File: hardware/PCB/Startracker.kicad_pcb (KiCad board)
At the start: 4 copper layers, 112 parts, among them IC1 IIS2MDCTR, IC2 BNO085, J1 GPS, J2 LoRa_prog, J3 Motor1, J4 Motor2, J5 Motor3, J6 6V, J7 SJ-3523-SMT-TR, J8 USB_C_Receptacle_USB2.0_16P, Q1 2N3904, Q2 2N3904, SW1 RST, SW2 BOOT, SW3 PWR, U1 ESP32-S3-WROOM-1, U10 TPS2121RUXR, U11 INA219BxDCN, U2 TMC2209-LA, U3 TB6612FNG, U4 TB6612FNG, U6 INA219BxDCN, U7 WLR089U0-I_RM, U8 SRV05-4, U9 TPS54308, Y1 Crystal

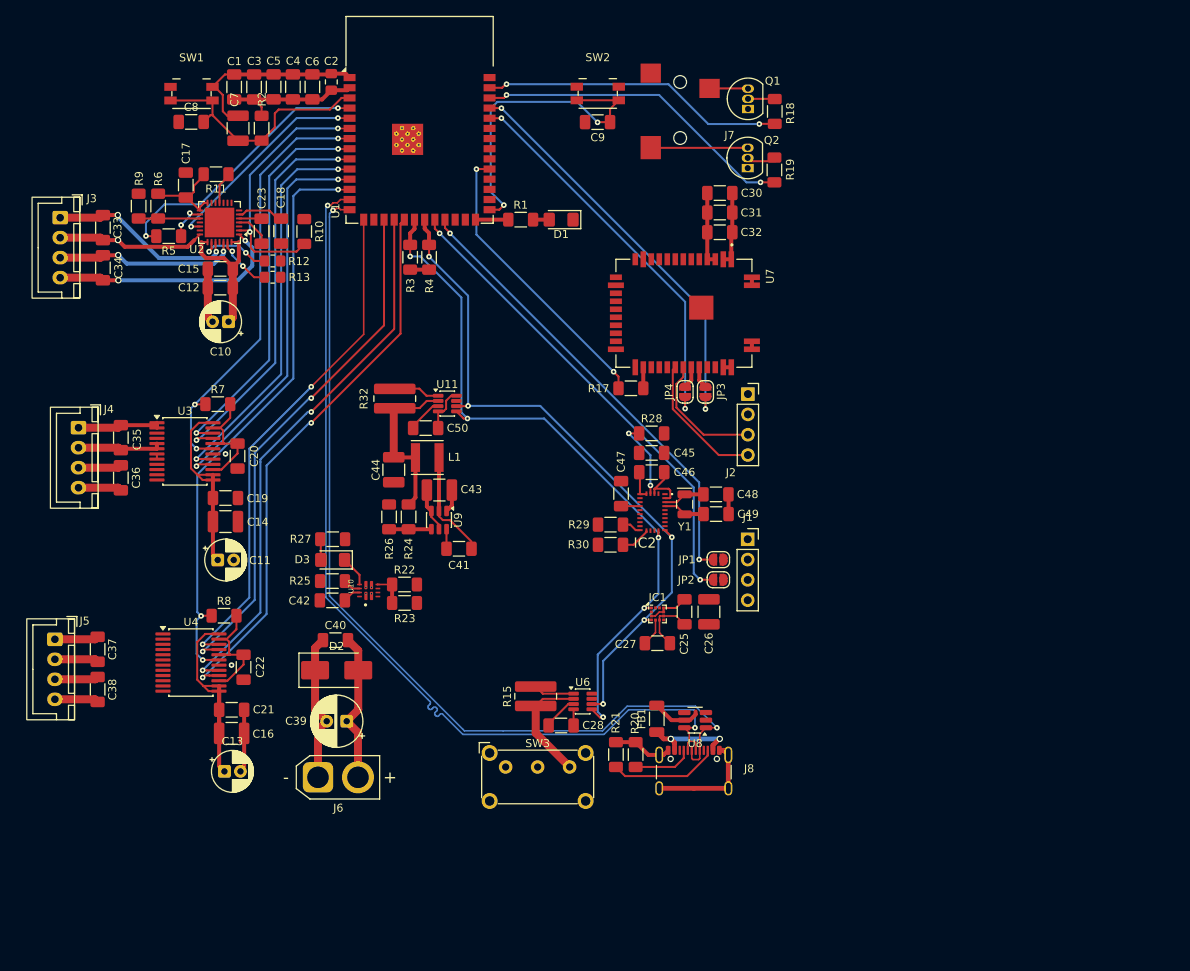
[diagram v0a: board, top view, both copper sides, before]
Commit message: Rerouted changes on the PCB layout, Routed LoRa
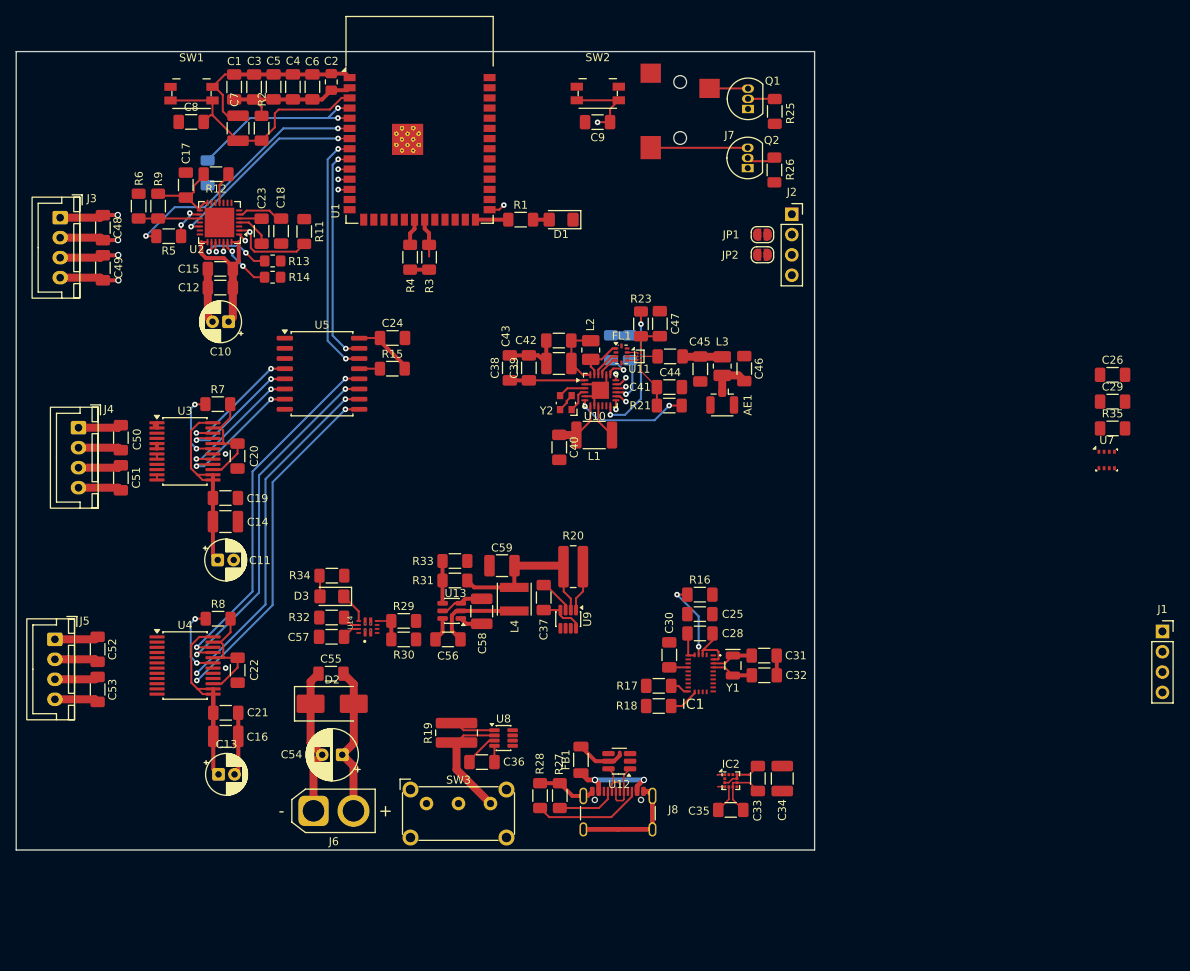
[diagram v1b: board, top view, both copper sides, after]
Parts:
- removed the C30 at (161.0, 53.7)
- removed the C31 at (161.0, 56.1)
- removed the C32 at (161.0, 58.6)
- removed the J2 at (164.5, 78.8)
- removed JP3, JP4: Jumper_2_Open, Jumper:SolderJumper-2_P1.3mm_Open_RoundedPad1.0x1.5mm
- removed the R17 at (149.9, 78.1)
- added AE1: uFL, Connector_Coaxial:U.FL_Hirose_U.FL-R-SMT-1_Vertical, F.Cu at (161.3, 79.7)
- added C24: 100n, Capacitor_SMD:C_1206_3216Metric_Pad1.33x1.80mm_HandSolder, F.Cu at (120.1, 71.8)
- added C26: 100n, Capacitor_SMD:C_1206_3216Metric_Pad1.33x1.80mm_HandSolder, F.Cu at (210.1, 76.4)
- added C29: 100n, Capacitor_SMD:C_1206_3216Metric_Pad1.33x1.80mm_HandSolder, F.Cu at (210.1, 79.7)
- added C38: 1u, Capacitor_SMD:C_1206_3216Metric_Pad1.33x1.80mm_HandSolder, F.Cu at (134.7, 75.5)
- added C39: 100n, Capacitor_SMD:C_1206_3216Metric_Pad1.33x1.80mm_HandSolder, F.Cu at (137.1, 75.5)
- added C40: 470n, Capacitor_SMD:C_1206_3216Metric_Pad1.33x1.80mm_HandSolder, F.Cu at (140.9, 85.4)
- added C41: 1n, Capacitor_SMD:C_1206_3216Metric_Pad1.33x1.80mm_HandSolder, F.Cu at (154.7, 77.9)
- added C42: 100n, Capacitor_SMD:C_1206_3216Metric_Pad1.33x1.80mm_HandSolder, F.Cu at (140.9, 72.1)
- added C43: 10u, Capacitor_SMD:C_1210_3225Metric_Pad1.33x2.70mm_HandSolder, F.Cu at (140.9, 75.0)
- added C44: 100p, Capacitor_SMD:C_1206_3216Metric_Pad1.33x1.80mm_HandSolder, F.Cu at (154.8, 74.1)
- added C45: 12p, Capacitor_SMD:C_1206_3216Metric_Pad1.33x1.80mm_HandSolder, F.Cu at (158.6, 75.7)
- added C46: DNP, Capacitor_SMD:C_1206_3216Metric_Pad1.33x1.80mm_HandSolder, F.Cu at (164.1, 75.6)
- added C47: 1n, Capacitor_SMD:C_1206_3216Metric_Pad1.33x1.80mm_HandSolder, F.Cu at (153.5, 70.0)
- added FL1: 0900FM15K0039, RF_Converter:Balun_Johanson_0900FM15K0039, F.Cu at (148.7, 73.8)
- added J1: GPS, Connector_PinSocket_2.54mm:PinSocket_1x04_P2.54mm_Vertical, F.Cu at (216.3, 108.5)
- added L1: 15uH, Inductor_SMD:L_1812_4532Metric_Pad1.30x3.40mm_HandSolder, F.Cu at (145.3, 83.9)
- added L2: 47n, Inductor_SMD:L_1008_2520Metric_Pad1.43x2.20mm_HandSolder, F.Cu at (144.9, 73.3)
- added L3: 8.2n, Inductor_SMD:L_1008_2520Metric_Pad1.43x2.20mm_HandSolder, F.Cu at (161.3, 75.3)
- added R10: 1k, Resistor_SMD:R_1206_3216Metric_Pad1.30x1.75mm_HandSolder, B.Cu at (97.0, 51.1)
- added R15: 10k, Resistor_SMD:R_1206_3216Metric_Pad1.30x1.75mm_HandSolder, F.Cu at (120.1, 75.6)
- added R21: 100, Resistor_SMD:R_1206_3216Metric_Pad1.30x1.75mm_HandSolder, F.Cu at (154.7, 80.2)
- added R22: 10k, Resistor_SMD:R_1206_3216Metric_Pad1.30x1.75mm_HandSolder, B.Cu at (149.8, 73.0)
- added R23: 100, Resistor_SMD:R_1206_3216Metric_Pad1.30x1.75mm_HandSolder, F.Cu at (151.1, 70.0)
- added R24: 10k, Resistor_SMD:R_1206_3216Metric_Pad1.30x1.75mm_HandSolder, B.Cu at (147.4, 73.0)
- added R35: 10k, Capacitor_SMD:C_1206_3216Metric_Pad1.33x1.80mm_HandSolder, F.Cu at (210.1, 83.1)
- added U10: SX1261IMLTRT, Package_DFN_QFN:QFN-24-1EP_4x4mm_P0.5mm_EP2.15x2.15mm, F.Cu at (146.1, 78.3)
- added U11: BGS12P2L6E6327XT, Package_LGA:Infineon_PG-TSNP-6-10_0.7x1.1mm_0.7x1.1mm_P0.4mm, F.Cu at (150.9, 74.1)
- added U5: PCF8574T, Package_SO:SOIC-16W_7.5x10.3mm_P1.27mm, F.Cu at (111.3, 76.3)
- added Y2: 32.00 MHz, saját:Crystal_SMD_Abracon_ABM10N-4Pin_2.5x2.0mm, F.Cu at (141.9, 79.9)
- U7: value WLR089U0-I_RM -> BME280; footprint WLR089U0-I_RM:MODULE_WLR089U0-I_RM -> Package_LGA:Bosch_LGA-8_2.5x2.5mm_P0.65mm_ClockwisePinNumbering
- moved U7 55.9 mm to (209.4, 87.0), turned to 0 degrees
- moved J2 41.0 mm to (170.0, 56.3)
- moved JP1 41.0 mm to (166.3, 58.9)
- moved JP2 41.0 mm to (166.3, 61.4)
- moved U9 30.9 mm to (142.1, 106.9), turned to -90 degrees
- moved R20 30.6 mm to (142.7, 100.4), turned to 180 degrees
- moved C37 25.8 mm to (139.0, 104.2), turned to -90 degrees
- moved C33 22.8 mm to (165.8, 126.8)
- moved C34 22.8 mm to (168.8, 126.8)
- moved C35 22.8 mm to (162.4, 130.8)
- moved IC2 22.8 mm to (162.4, 127.1)
- moved C31 21.0 mm to (166.5, 111.5)
- moved C28 21.0 mm to (158.5, 108.7)
- moved C30 21.0 mm to (154.7, 111.4)
- moved C32 21.0 mm to (166.6, 113.9)
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- renumbered C45 to C25, C46 to C28, C47 to C30, C48 to C31, C49 to C32, C25 to C33, C26 to C34, C27 to C35, C28 to C36, C50 to C37, C33 to C48, C34 to C49, C35 to C50, C36 to C51, C37 to C52, C38 to C53, C39 to C54, C40 to C55, C41 to C56, C42 to C57, C43 to C58, C44 to C59, IC2 to IC1, IC1 to IC2, J1 to J2, L1 to L4, R10 to R11, R11 to R12, R12 to R13, R13 to R14, R28 to R16, R29 to R17, R30 to R18, R15 to R19, R32 to R20, R18 to R25, R19 to R26, R20 to R27, R21 to R28, R22 to R29, R4 to R3, R23 to R30, R24 to R31, R25 to R32, R26 to R33, R27 to R34, R3 to R4, R9 to R6, R6 to R9, U8 to U12, U9 to U13, U10 to U14, U6 to U8, U11 to U9
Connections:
- C48 pad 2: /CONN/M1_A- -> /CONN/M1_B+
- C49 pad 2: /CONN/M1_B+ -> /CONN/M1_A-
- C50 pad 2: /CONN/M2_A2 -> /CONN/M2_B1
- C51 pad 2: /CONN/M2_B1 -> /CONN/M2_A2
- C52 pad 2: /CONN/M3_A2 -> /CONN/M3_B1
- C53 pad 2: /CONN/M3_B1 -> /CONN/M3_A2
- IC1 pad 11: BNO_RST -> Net-(IC1-NRST)
- J3 pad 2: /CONN/M1_A- -> /CONN/M1_B+
- J3 pad 3: /CONN/M1_B+ -> /CONN/M1_A-
- J4 pad 2: /CONN/M2_A2 -> /CONN/M2_B1
- J4 pad 3: /CONN/M2_B1 -> /CONN/M2_A2
- J5 pad 2: /CONN/M3_A2 -> /CONN/M3_B1
- J5 pad 3: /CONN/M3_B1 -> /CONN/M3_A2
- R11 pad 1: /Motor driver/D1_EN -> Net-(U2-~{EN})
- R6 pad 1: GND -> Net-(U2-VREF)
- R6 pad 2: Net-(U2-VREF) -> +3.3V
- R7 pad 1: /Motor driver/D2_STBY -> Net-(U3-STBY)
- R8 pad 1: /Motor driver/D3_STBY -> Net-(U4-STBY)
- R9 pad 1: Net-(U2-VREF) -> GND
- R9 pad 2: +3.3V -> Net-(U2-VREF)
- U1 pad 10: /Motor driver/D2_B1 -> /OBC/I2C_SCL
- U1 pad 11: /Motor driver/D2_B2 -> /OBC/I2C_SDA
- U1 pad 12: /Motor driver/D3_STBY -> unconnected-(U1-IO8-Pad12)
- U1 pad 15: /Motor driver/D3_A2 -> unconnected-(U1-IO3-Pad15)
- U1 pad 17: /Motor driver/D3_A1 -> /LORA/SX_RST
- U1 pad 18: /Motor driver/D3_B1 -> /LORA/SX_SCK
- U1 pad 19: /Motor driver/D3_B2 -> /LORA/SX_MOSI
- U1 pad 20: /OBC/I2C_SCL -> /LORA/SX_MISO
- U1 pad 21: /OBC/I2C_SDA -> /LORA/SX_NSS
- U1 pad 22: /OBC/GPS_RX -> /LORA/SX_DIO1
- U1 pad 23: /OBC/GPS_TX -> /LORA/SX_BUSY
- U1 pad 31: /LORA/LORA_RST -> unconnected-(U1-IO38-Pad31)
- U1 pad 36: /LORA/RXD -> /OBC/GPS_RX
- U1 pad 37: /LORA/TXD -> /OBC/GPS_TX
- U1 pad 4: /Motor driver/STEP1 -> /Motor driver/TMC_RX
- U1 pad 5: /Motor driver/DIR1 -> /Motor driver/TMC_RX
- U1 pad 6: /Motor driver/D1_EN -> /Motor driver/STEP1
- U1 pad 7: /Motor driver/D2_STBY -> /Motor driver/DIR1
- U1 pad 8: /Motor driver/D2_A2 -> /Motor driver/TB_SCL
- U1 pad 9: /Motor driver/D2_A1 -> /Motor driver/TB_SDA
- U2 pad 10: +3.3V -> GND
- U2 pad 14: +3.3V -> Net-(U2-~{PD}/UART)
- U2 pad 2: /Motor driver/D1_EN -> Net-(U2-~{EN})
- U2 pad 9: GND -> +3.3V
- U3 pad 16: /Motor driver/D2_B2 -> D2_B2
- U3 pad 17: /Motor driver/D2_B1 -> D2_B1
- U3 pad 19: /Motor driver/D2_STBY -> Net-(U3-STBY)
- U3 pad 21: /Motor driver/D2_A1 -> D2_A1
- U3 pad 22: /Motor driver/D2_A2 -> D2_A2
- U4 pad 16: /Motor driver/D3_B2 -> D3_B2
- U4 pad 17: /Motor driver/D3_B1 -> D3_B1
- U4 pad 19: /Motor driver/D3_STBY -> Net-(U4-STBY)
- U4 pad 21: /Motor driver/D3_A1 -> D3_A1
- U4 pad 22: /Motor driver/D3_A2 -> D3_A2
- U7 pad 1: GND -> GND_1
- U7 pad 2: GND -> +3.3V
- U7 pad 4: +3.3V -> /OBC/I2C_SCL
- U7 pad 5: unconnected-(U7-PA07-Pad5) -> /OBC/I2C_SDA
- U7 pad 6: unconnected-(U7-PA08-Pad6) -> +3.3V
- U7 pad 7: unconnected-(U7-PA27-Pad7) -> GND_1
- U7 pad 8: unconnected-(U7-PA16-Pad8) -> +3.3V
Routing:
- net /OBC/USB_D-: track 117.2 -> 5.06 mm, vias 2 -> 0
- net /OBC/USB_D+: track 116.1 -> 6.25 mm, vias 2 -> 0
- net /OBC/I2C_SCL: track 90.5 -> 5.72 mm, vias 5 -> 1
- net /OBC/I2C_SDA: track 87.2 -> 7.15 mm, vias 5 -> 1
- net /Motor driver/D3_STBY: track 74.5 -> 0.00 mm, vias 3 -> 0
- net /Motor driver/D3_A2: track 74.4 -> 0.00 mm, vias 2 -> 0
- net /Motor driver/D3_B2: track 69.8 -> 0.00 mm, vias 2 -> 0
- net /Motor driver/D3_B1: track 68.5 -> 0.00 mm, vias 2 -> 0
- net /Motor driver/D3_A1: track 65.7 -> 0.00 mm, vias 2 -> 0
- net /OBC/GPS_RX: track 60.4 -> 0.00 mm, vias 2 -> 0
- net /OBC/GPS_TX: track 57.4 -> 0.00 mm, vias 2 -> 0
- net /Motor driver/D2_STBY: track 54.5 -> 0.00 mm, vias 3 -> 0
- net /LORA/TXD: track 51.2 -> 0.00 mm, vias 2 -> 0
- net /Motor driver/D2_B1: track 50.1 -> 0.00 mm, vias 2 -> 0
- net /Motor driver/D2_B2: track 49.9 -> 0.00 mm, vias 2 -> 0
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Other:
- board outline added: 99.8 x 99.8 mm

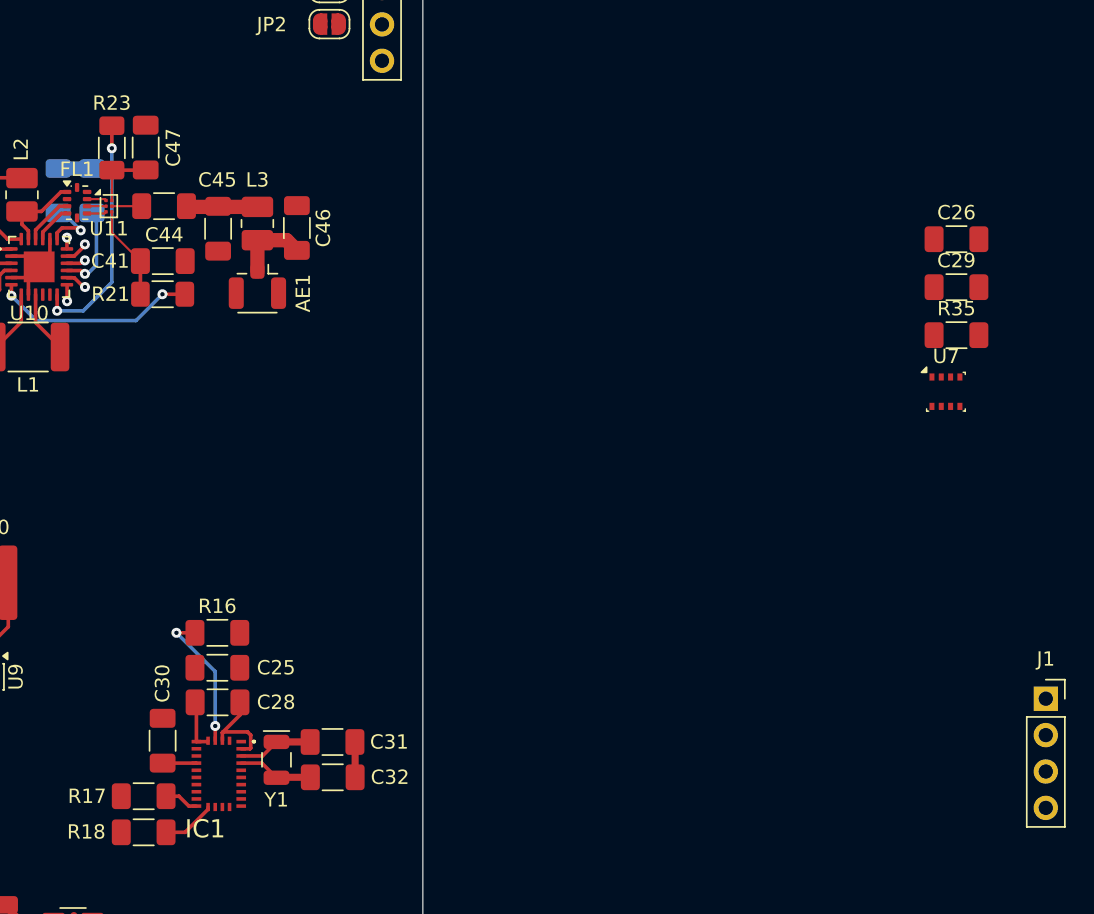
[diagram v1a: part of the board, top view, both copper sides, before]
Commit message: Completed placement of components on PCB
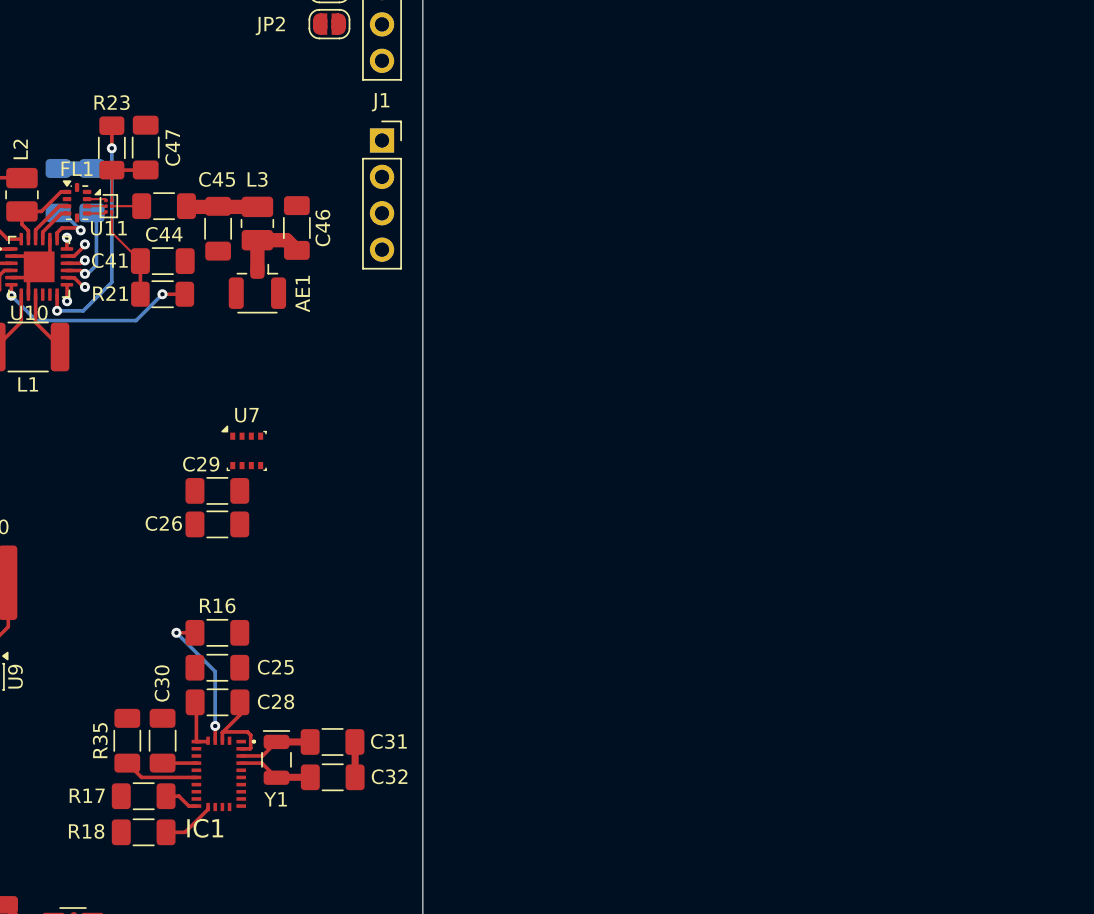
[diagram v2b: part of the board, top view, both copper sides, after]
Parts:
- J1: value GPS -> IMU_EXT
- moved R35 64.4 mm to (152.2, 111.4), turned to 90 degrees
- moved J1 60.5 mm to (170.0, 69.5)
- moved C26 55.3 mm to (158.5, 96.3)
- moved C29 53.5 mm to (158.5, 94.0)
- moved U7 49.0 mm to (160.6, 91.2)
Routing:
- net Net-(IC1-NRST): track 0.00 -> 5.24 mm
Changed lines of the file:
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@@
 	(footprint "Connector_PinSocket_2.54mm:PinSocket_1x04_P2.54mm_Vertical"
 		(layer "F.Cu")
-		(at 216.3318 108.458)
+		(at 170.0022 69.4944)
 		(descr "Through hole straight socket strip, 1x04, 2.54mm pitch, single row (from Kicad 4.0.7), script generated")
 		(tags "Through hole socket strip THT 1x04 2.54mm single row")
@@
 			)
 		)
-		(property "Value" "GPS"
+		(property "Value" "IMU_EXT"
 			(at 0 10.39 0)
 			(layer "F.Fab")
+			(hide yes)
 			(effects
 				(font
@@
 	(footprint "Capacitor_SMD:C_1206_3216Metric_Pad1.33x1.80mm_HandSolder"
 		(layer "F.Cu")
-		(at 210.0965 79.7334)
+		(at 158.5091 93.9546)
 		(descr "Capacitor SMD 1206 (3216 Metric), square (rectangular) end terminal, IPC-7351 nominal with elongated pad for handsoldering. (Body size source: IPC-SM-782 page 76, https://www.pcb-3d.com/wordpress/wp-content/uploads/ipc-sm-782a_amendment_1_and_2.pdf), generated with kicad-footprint-generator")
 		(tags "capacitor handsolder")
 		(property "Reference" "C29"
-			(at 0 -1.85 0)
+			(at -1.1176 -1.8288 0)
 			(layer "F.SilkS")
 			(effects
@@
 			(at 0 1.85 0)
 			(layer "F.Fab")
+			(hide yes)
 			(effects
 				(font
@@
 	(footprint "Capacitor_SMD:C_1206_3216Metric_Pad1.33x1.80mm_HandSolder"
 		(layer "F.Cu")
-		(at 210.0965 76.3834)
+		(at 158.5091 96.2914)
 		(descr "Capacitor SMD 1206 (3216 Metric), square (rectangular) end terminal, IPC-7351 nominal with elongated pad for handsoldering. (Body size source: IPC-SM-782 page 76, https://www.pcb-3d.com/wordpress/wp-content/uploads/ipc-sm-782a_amendment_1_and_2.pdf), generated with kicad-footprint-generator")
 		(tags "capacitor handsolder")
 		(property "Reference" "C26"
-			(at 0 -1.85 0)
+			(at -3.7338 -0.0254 0)
 			(layer "F.SilkS")
 			(effects
@@
 			(at 0 1.85 0)
 			(layer "F.Fab")
+			(hide yes)
 			(effects
 				(font
@@
 	(footprint "Capacitor_SMD:C_1206_3216Metric_Pad1.33x1.80mm_HandSolder"
 		(layer "F.Cu")
-		(at 210.0965 83.0834)
+		(at 152.2222 111.3913 90)
 		(descr "Capacitor SMD 1206 (3216 Metric), square (rectangular) end terminal, IPC-7351 nominal with elongated pad for handsoldering. (Body size source: IPC-SM-782 page 76, https://www.pcb-3d.com/wordpress/wp-content/uploads/ipc-sm-782a_amendment_1_and_2.pdf), generated with kicad-footprint-generator")
 		(tags "capacitor handsolder")
 		(property "Reference" "R35"
-			(at 0 -1.85 0)
+			(at 0 -1.85 90)
 			(layer "F.SilkS")
 			(effects
@@
 		)
 		(property "Value" "10k"
-			(at 0 1.85 0)
+			(at 0 1.85 90)
 			(layer "F.Fab")
+			(hide yes)
 			(effects
 				(font
@@
 		)
 		(property "Datasheet" "~"
-			(at 0 0 0)
+			(at 0 0 90)
 			(layer "F.Fab")
 			(hide yes)
@@
 		)
 		(property "Description" "Resistor"
-			(at 0 0 0)
+			(at 0 0 90)
 			(layer "F.Fab")
 			(hide yes)
@@
 		)
 		(property "Sim.Device" ""
-			(at 0 0 0)
+			(at 0 0 90)
 			(unlocked yes)
 			(layer "F.Fab")
@@
 		)
 		(property "TAPE_REEL" ""
-			(at 0 0 0)
+			(at 0 0 90)
 			(unlocked yes)
 			(layer "F.Fab")
@@
 		)
 		(property "VOLUME" ""
-			(at 0 0 0)
+			(at 0 0 90)
 			(unlocked yes)
 			(layer "F.Fab")
@@
 		)
 		(fp_text user "${REFERENCE}"
-			(at 0 0 0)
+			(at 0 0 90)
 			(layer "F.Fab")
 			(effects
@@
 		)
 		(pad "1" smd roundrect
-			(at -1.5625 0)
+			(at -1.5625 0 90)
 			(size 1.325 1.8)
 			(layers "F.Cu" "F.Mask" "F.Paste")
@@
 		)
 		(pad "2" smd roundrect
-			(at 1.5625 0)
+			(at 1.5625 0 90)
 			(size 1.325 1.8)
 			(layers "F.Cu" "F.Mask" "F.Paste")
@@
 	(footprint "Package_LGA:Bosch_LGA-8_2.5x2.5mm_P0.65mm_ClockwisePinNumbering"
 		(layer "F.Cu")
-		(at 209.3615 87.0284)
+		(at 160.5562 91.1615)
 		(descr "LGA-8")
 		(tags "lga land grid array")
@@
 			(at 0.015 2.535 0)
 			(layer "F.Fab")
+			(hide yes)
 			(effects
 				(font
@@
 	)
 	(segment
+		(start 157.0464 113.9538)
+		(end 153.2222 113.9538)
+		(width 0.254)
+		(layer "F.Cu")
+		(net 94)
+	)
+	(segment
+		(start 153.2222 113.9538)
+		(end 152.2222 112.9538)
+		(width 0.254)
+		(layer "F.Cu")
+		(net 94)
+	)
+	(segment

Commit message: Finished routing and layout of PCB
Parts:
- U1: footprint RF_Module:ESP32-S3-WROOM-1 -> saját:sa
- moved R6 24.4 mm to (108.9, 68.4), turned to 90 degrees
- moved L1 22.9 mm to (163.4, 97.9)
- moved C40 22.9 mm to (159.1, 99.4)
- moved C13 22.4 mm to (116.5, 139.4)
- moved C26 22.4 mm to (176.6, 109.4)
- moved C35 22.4 mm to (180.5, 143.9)
- moved C36 22.4 mm to (149.4, 137.9)
- moved C37 22.4 mm to (157.1, 117.3)
- moved C41 22.4 mm to (172.8, 91.0)
- moved C59 22.4 mm to (151.9, 113.4)
- moved FB1 22.4 mm to (161.8, 137.6)
- moved JP1 22.4 mm to (184.5, 72.0)
- moved R11 22.4 mm to (127.2, 71.6)
- moved R17 22.4 mm to (171.5, 128.4)
- moved R19 22.4 mm to (146.2, 134.2)
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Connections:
- C26 pad 1: GND_1 -> GND
- C29 pad 1: GND_1 -> GND
- C33 pad 1: GND_1 -> GND
- C34 pad 1: GND_1 -> GND
- C35 pad 2: GND_1 -> GND
- C36 pad 1: GND_1 -> GND
- C37 pad 1: GND_1 -> GND
- IC2 pad 6: GND_1 -> GND
- IC2 pad 8: GND_1 -> GND
- R3 pad 1: /OBC/I2C_SDA -> /OBC/I2C_SCL
- R4 pad 1: /OBC/I2C_SCL -> /OBC/I2C_SDA
- U1 pad 10: /OBC/I2C_SCL -> /OBC/I2C_SDA
- U1 pad 11: /OBC/I2C_SDA -> /OBC/I2C_SCL
- U1 pad 17: /LORA/SX_RST -> /LORA/SX_DIO1
- U1 pad 18: /LORA/SX_SCK -> /LORA/SX_BUSY
- U1 pad 19: /LORA/SX_MOSI -> /LORA/SX_RST
- U1 pad 21: /LORA/SX_NSS -> /LORA/SX_MOSI
- U1 pad 22: /LORA/SX_DIO1 -> /LORA/SX_SCK
- U1 pad 23: /LORA/SX_BUSY -> /LORA/SX_NSS
- U7 pad 1: GND_1 -> GND
- U7 pad 7: GND_1 -> GND
- U8 pad 3: GND_1 -> GND
- U8 pad 7: GND_1 -> GND
- U8 pad 8: GND_1 -> GND
- U9 pad 3: GND_1 -> GND
- U9 pad 7: GND_1 -> GND
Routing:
- net +3.3V: track 110.1 -> 458.6 mm, vias 0 -> 2
- net /OBC/I2C_SCL: track 5.72 -> 187.9 mm, vias 1 -> 5
- net /OBC/I2C_SDA: track 7.15 -> 188.0 mm, vias 1 -> 6
- net /OBC/USB_D-: track 5.06 -> 106.3 mm, vias 0 -> 2
- net /OBC/USB_D+: track 6.25 -> 105.3 mm, vias 0 -> 2
- net VM: track 77.6 -> 163.8 mm
- net GND: track 107.3 -> 187.7 mm, vias 2 -> 88
- net /CONN/Focus: track 0.00 -> 46.1 mm, vias 0 -> 2
- net /CONN/Shutter: track 0.00 -> 41.7 mm, vias 0 -> 2
- net /OBC/GPS_RX: track 0.00 -> 40.6 mm, vias 0 -> 2
- net /OBC/GPS_TX: track 0.00 -> 40.0 mm, vias 0 -> 2
- net /LORA/SX_DIO1: track 1.12 -> 40.7 mm, vias 1 -> 2
- net /LORA/SX_BUSY: track 1.42 -> 40.6 mm, vias 1 -> 2
- net /LORA/SX_RST: track 6.03 -> 43.5 mm, vias 1 -> 2
- net /LORA/SX_MISO: track 1.21 -> 37.1 mm, vias 1 -> 2
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- added copper zone on B.Cu, net GND
- added copper zone on F.Cu, net GND
- added copper zone on In1.Cu, net GND
- added copper zone on In2.Cu, net GND
